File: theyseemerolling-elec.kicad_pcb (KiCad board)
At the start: 2 copper layers, 80 x 50 mm, 88 parts, among them IC2 L6205PD, J1 Conn_Encoder1, J2 Conn_Power_In, J3 Conn_SWD_UART, J4 Conn_Mot1, J5 Conn_Mot2, J6 Conn_Encoder2, J7 CAN_conn, J8 CAN_conn, Q1 BSS138, Q2 BSS138, Q3 BSS138, Q4 BSS138, Q5 BSS138, U1 STM32F303K8Tx, U2 LD1117S50TR_SOT223, U3 ACS711xLCTR-12AB, U4 ACS711xLCTR-12AB, U5 74HC00, U6 LD1117S33TR_SOT223, U7 TCAN332, U8 AT25SF041

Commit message: prettier
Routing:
- net +3V3: track 213.2 -> 210.8 mm
- net +5V: track 72.1 -> 70.4 mm
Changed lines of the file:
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@@
     (thickness 1.6)
     (drawings 13)
-    (tracks 573)
+    (tracks 575)
     (zones 0)
     (modules 88)
@@
   )
   (setup
-    (last_trace_width 0.25)
+    (last_trace_width 0.5)
     (user_trace_width 0.5)
     (user_trace_width 1)
@@
   (segment (start 165.8 72.4) (end 166.6 72.4) (width 1) (layer F.Cu) (net 15) (status 30))
   (segment (start 163.399989 69.999989) (end 165.8 72.4) (width 1) (layer F.Cu) (net 15) (status 20))
-  (via (at 132.19 78.3) (size 0.8) (drill 0.4) (layers F.Cu B.Cu) (net 16) (status 30))
-  (segment (start 127.975 68.8) (end 123.575 73.2) (width 0.5) (layer B.Cu) (net 16))
   (segment (start 143.8 63.8) (end 138.8 68.8) (width 0.5) (layer B.Cu) (net 16))
   (segment (start 143.8 63.8) (end 158.2 63.8) (width 0.5) (layer B.Cu) (net 16))
-  (segment (start 131.5375 78.3) (end 132.19 78.3) (width 0.25) (layer F.Cu) (net 16) (status 20))
-  (segment (start 130.1375 79.7) (end 131.5375 78.3) (width 0.25) (layer F.Cu) (net 16) (status 10))
-  (segment (start 130.1 79.7) (end 130.1375 79.7) (width 0.25) (layer F.Cu) (net 16) (status 30))
-  (segment (start 128.675 78.3) (end 132.19 78.3) (width 0.5) (layer B.Cu) (net 16))
-  (segment (start 123.575 73.2) (end 128.675 78.3) (width 0.5) (layer B.Cu) (net 16))
   (via (at 167.6 60.425) (size 0.8) (drill 0.4) (layers F.Cu B.Cu) (net 16) (status 30))
   (segment (start 166.1 60.905) (end 167.12 60.905) (width 0.5) (layer F.Cu) (net 16) (status 10))
@@
   (segment (start 127.975 64.425) (end 128.375 64.025) (width 0.5) (layer B.Cu) (net 16))
   (segment (start 128.375 64.025) (end 128.4 64.025) (width 0.5) (layer B.Cu) (net 16))
+  (segment (start 130.1 79.7) (end 130.1375 79.7) (width 0.25) (layer F.Cu) (net 16) (status 30))
+  (segment (start 130.1375 79.7) (end 131.5375 78.3) (width 0.25) (layer F.Cu) (net 16) (status 10))
+  (segment (start 131.5375 78.3) (end 132.19 78.3) (width 0.25) (layer F.Cu) (net 16) (status 20))
+  (via (at 130.1 79.7) (size 0.8) (drill 0.4) (layers F.Cu B.Cu) (net 16))
+  (segment (start 124.675216 73.975216) (end 130.1 79.4) (width 0.5) (layer B.Cu) (net 16))
+  (segment (start 130.1 79.4) (end 130.1 79.7) (width 0.5) (layer B.Cu) (net 16))
+  (segment (start 124.675216 72.099784) (end 127.975 68.8) (width 0.5) (layer B.Cu) (net 16))
+  (segment (start 124.675216 73.975216) (end 124.675216 72.099784) (width 0.5) (layer B.Cu) (net 16))
   (segment (start 107.725 62.2875) (end 107.2125 62.8) (width 1) (layer B.Cu) (net 17) (status 30))
   (segment (start 107.5 66.275) (end 107.425 66.2) (width 1) (layer B.Cu) (net 17) (status 30))
@@
   (segment (start 130.7 91.5375) (end 124.9625 91.5375) (width 1) (layer B.Cu) (net 19) (status 10))
   (segment (start 135.2625 91.5375) (end 135.2 91.6) (width 1) (layer B.Cu) (net 19) (status 30))
-  (segment (start 142 91.5375) (end 135.2625 91.5375) (width 1) (layer B.Cu) (net 19) (status 20))
   (segment (start 135.1375 91.5375) (end 135.2 91.6) (width 1) (layer B.Cu) (net 19) (status 30))
   (segment (start 130.7 91.5375) (end 135.1375 91.5375) (width 1) (layer B.Cu) (net 19) (status 30))
@@
   (segment (start 105.2 75.35) (end 105.2 73.2) (width 1) (layer B.Cu) (net 19) (status 10))
   (via (at 107 71.4) (size 0.8) (drill 0.4) (layers F.Cu B.Cu) (net 19) (status 30))
+  (segment (start 135.3625 91.4375) (end 135.2 91.6) (width 1) (layer B.Cu) (net 19))
+  (segment (start 140.2 91.4375) (end 135.3625 91.4375) (width 1) (layer B.Cu) (net 19))
   (segment (start 133.2 70.8) (end 125.6 78.4) (width 0.25) (layer F.Cu) (net 20))
   (segment (start 125.6 78.4) (end 124.75 78.4) (width 0.25) (layer F.Cu) (net 20) (status 20))

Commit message: Références
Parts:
- moved LOGO2 2.45 mm to (156.2, 59.8)

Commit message: Add text
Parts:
- moved C6 1.60 mm to (134.6, 64.6)
- moved D5 1.60 mm to (136.8, 64.6)
- moved Q1 1.60 mm to (131.4, 64.6)
- moved R16 1.60 mm to (128.4, 64.6)
- moved R2 1.60 mm to (135.8, 67.8)
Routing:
- net +3V3: track 210.8 -> 209.2 mm
- net /f3/ABOUT_DA_POWER: track 33.1 -> 32.4 mm
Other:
- board text added: "CAN"
- board text added: "Coder1"
- board text added: "Coder2"
- board text added: "Motor1"
- board text added: "Motor2"
- board text added: "Power In"
- board text added: "SWD+UART"

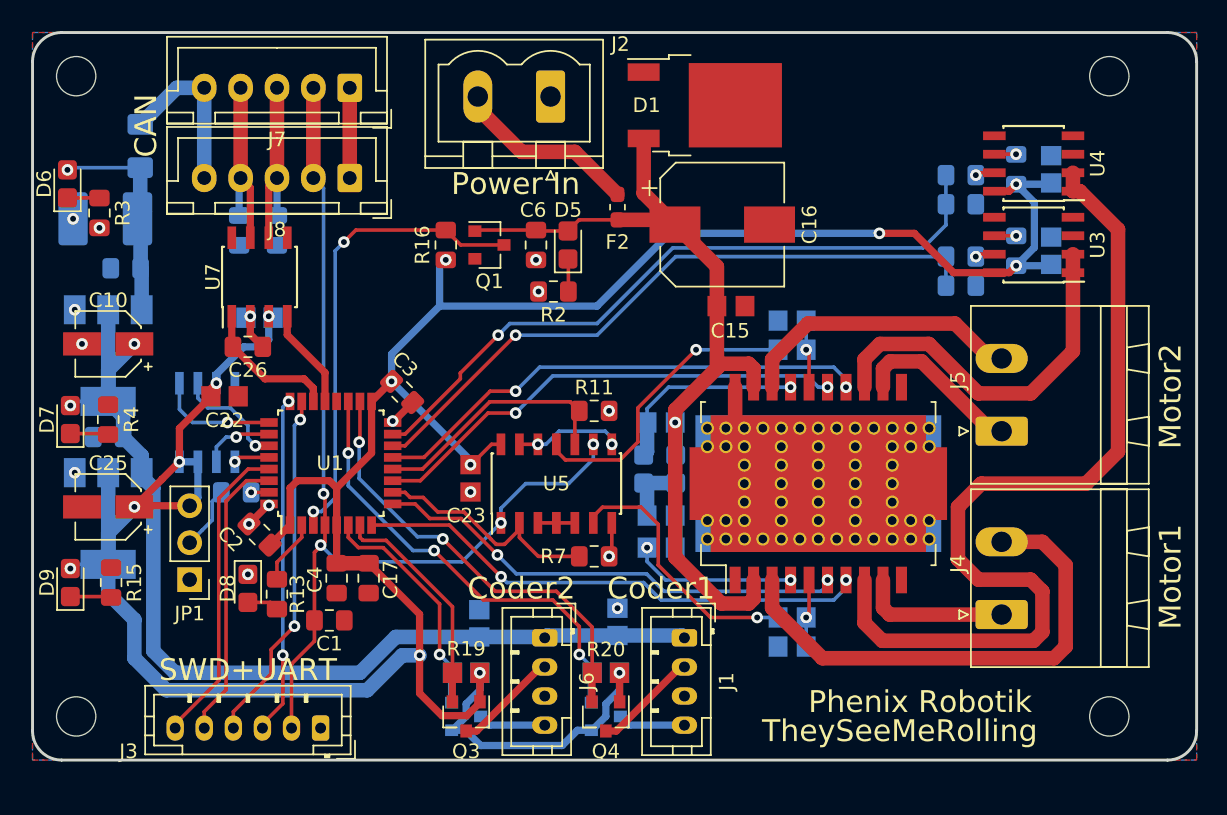
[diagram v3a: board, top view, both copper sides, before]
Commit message: Change connectors. reduce size.
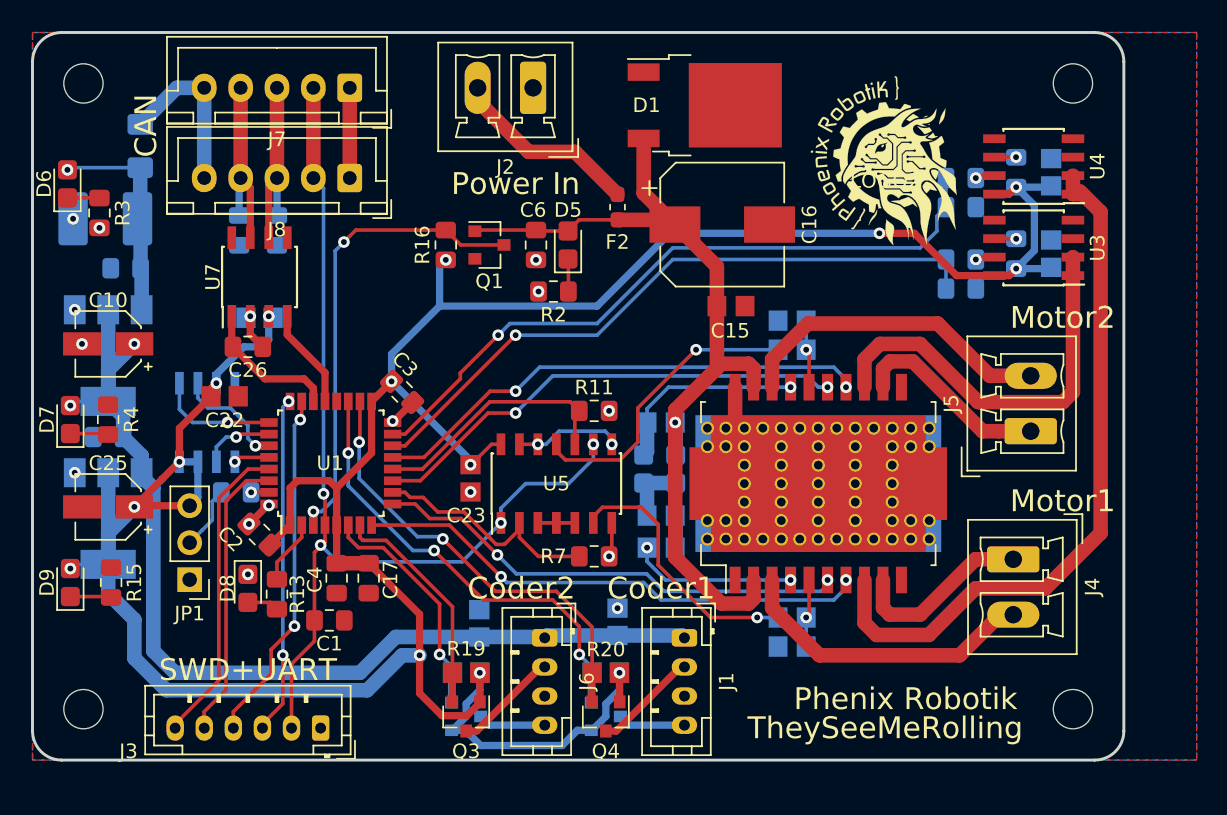
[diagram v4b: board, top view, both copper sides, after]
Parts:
- J2: footprint Connector_Phoenix_MSTB:PhoenixContact_MSTBVA_2,5_2-G_1x02_P5.00mm_Vertical -> Connector_Phoenix_MC:PhoenixContact_MCV_1,5_2-G-3.81_1x02_P3.81mm_Vertical
- J4, J5: footprint Connector_Phoenix_MSTB:PhoenixContact_MSTBA_2,5_2-G_1x02_P5.00mm_Horizontal -> Connector_Phoenix_MC:PhoenixContact_MCV_1,5_2-G-3.81_1x02_P3.81mm_Vertical
- LOGO2: moved to F.Cu
- moved J4 3.88 mm to (167.4, 86.2), turned to 270 degrees
- moved MK2 2.55 mm to (171.5, 53.5)
- moved MK3 2.55 mm to (171.5, 96.5)
- moved LOGO2 2.43 mm to (158.6, 60.2), turned to 0 degrees
- moved J5 2.00 mm to (168.6, 77.4)
- moved J2 1.34 mm to (134.4, 53.8)
- moved MK1 0.71 mm to (103.5, 53.5)
- moved MK4 0.71 mm to (103.5, 96.5)
- moved C20 0.20 mm to (170.0, 65.2)
- moved C21 0.20 mm to (170.0, 59.6)
- moved C9 0.20 mm to (163.8, 62.0)
- moved R14 0.20 mm to (163.8, 60.0)
- moved R5 0.20 mm to (167.6, 65.2)
- moved R6 0.20 mm to (167.6, 59.6)
- moved U3 0.20 mm to (168.8, 64.8)
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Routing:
- net Net-(IC2-Pad8): track 62.3 -> 48.2 mm
- net /DualDCDriver/M1-: track 34.5 -> 21.0 mm
- net /DualDCDriver/M2-: track 19.7 -> 22.2 mm
- net /DualDCDriver/M1+: track 10.3 -> 12.6 mm
- net Net-(IC2-Pad13): track 26.0 -> 28.1 mm
- net /DualDCDriver/M2+: track 11.6 -> 13.6 mm
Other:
- board size 80 x 50 mm -> 75 x 50 mm

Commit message: fix phoenix/phenix
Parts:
- LOGO2: footprint PhoenixRobotik:Logo_14,5mm -> PhenixRobotik:Logo_14,5mm
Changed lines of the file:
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@@
     )
   )
-  (module PhoenixRobotik:Logo_14,5mm (layer F.Cu)
+  (module PhenixRobotik:Logo_14,5mm (layer F.Cu)
     (at 158.6 60.2)
     (descr https://github.com/PhenixRobotik)

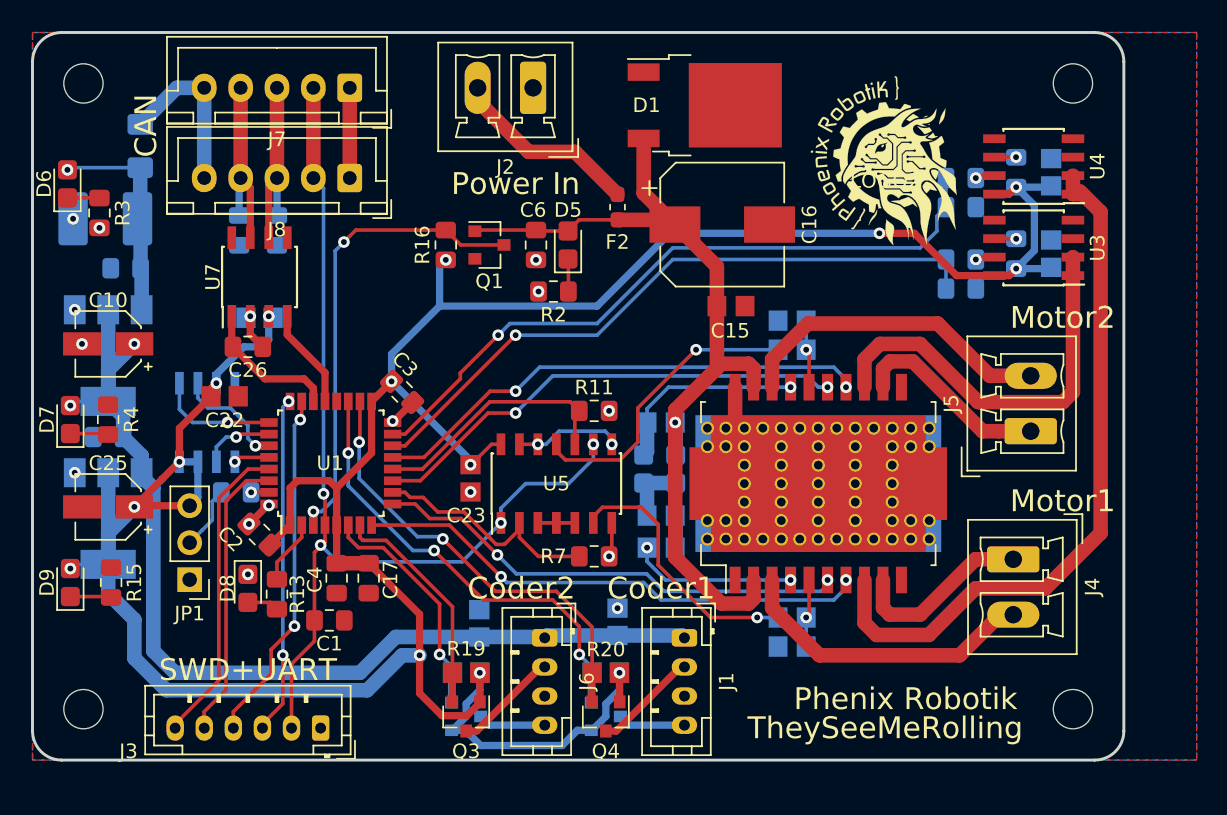
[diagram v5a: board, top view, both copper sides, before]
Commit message: Fix : use new footprints
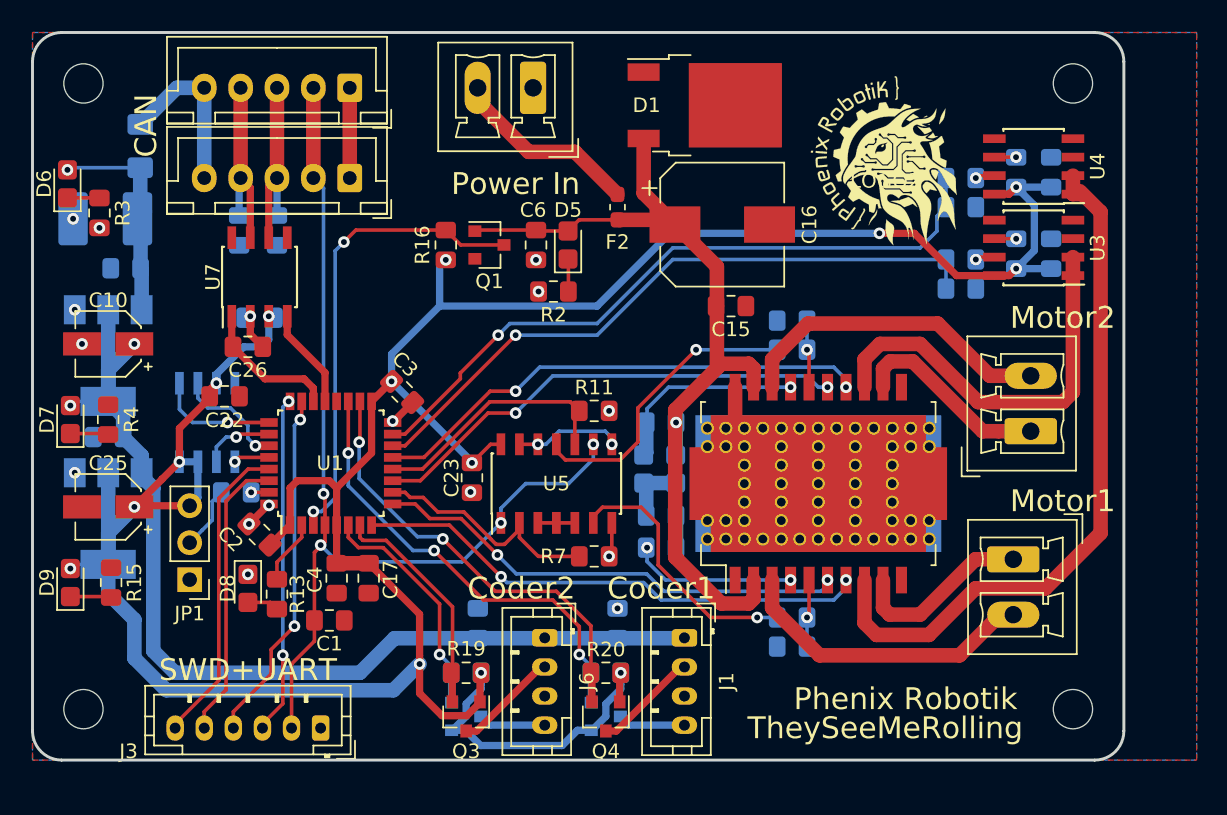
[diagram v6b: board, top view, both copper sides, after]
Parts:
- C11, C12, C13, C14, C15: footprint Capacitor_SMD:C_0805_2012Metric_Pad1.29x1.40mm_HandSolder -> Capacitor_SMD:C_0805_2012Metric_Pad1.15x1.40mm_HandSolder
- C18, C19, C20, C21, C22, C23, C24: footprint Capacitor_SMD:C_0805_2012Metric_Pad1.33x1.40mm_HandSolder -> Capacitor_SMD:C_0805_2012Metric_Pad1.15x1.40mm_HandSolder
- R10, R8, R9: footprint Resistor_SMD:R_0805_2012Metric_Pad1.29x1.40mm_HandSolder -> Resistor_SMD:R_0805_2012Metric_Pad1.15x1.40mm_HandSolder
- R18, R19, R20, R21: footprint Resistor_SMD:R_0805_2012Metric_Pad1.33x1.40mm_HandSolder -> Resistor_SMD:R_0805_2012Metric_Pad1.15x1.40mm_HandSolder
- moved C23 0.11 mm to (130.2, 80.6)
- moved C18 0.10 mm to (140.2, 90.6)
- moved C19 0.10 mm to (130.6, 90.6)

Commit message: Cleanup, check footprints, connect mounting holes to GND
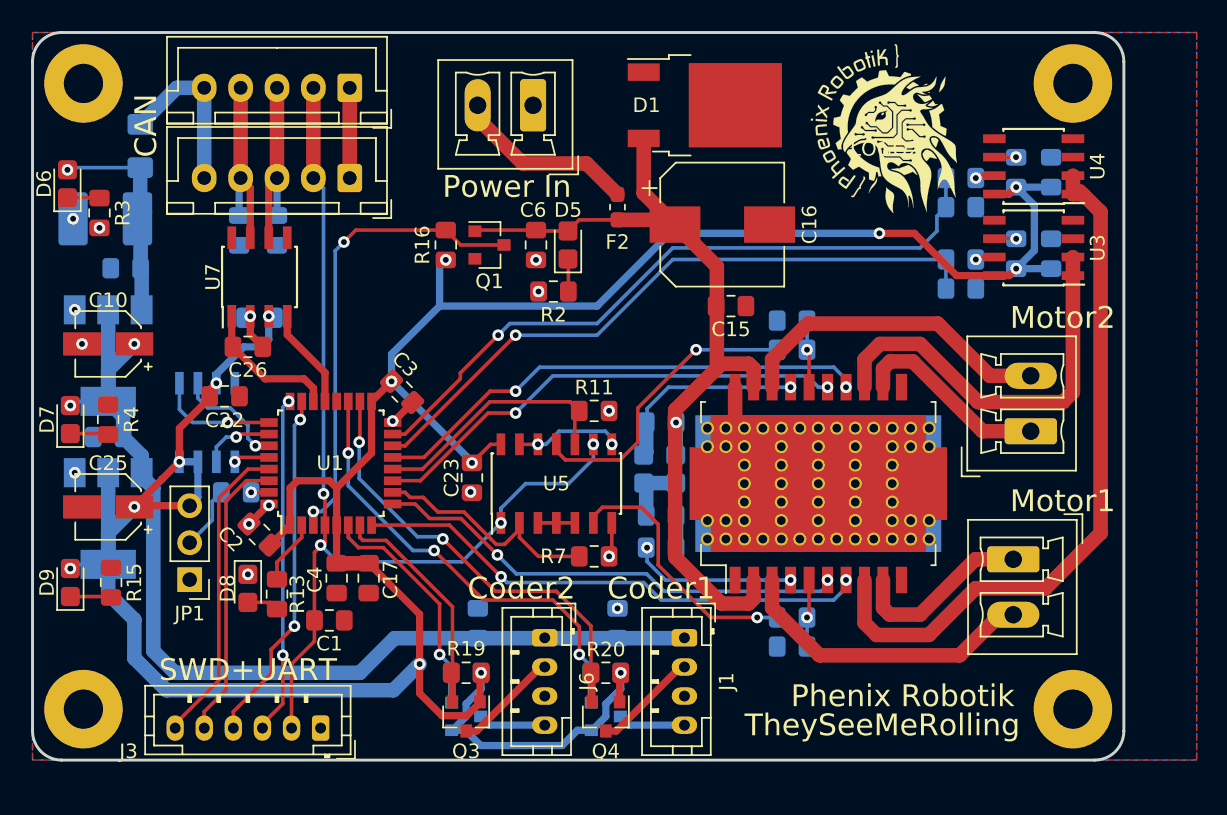
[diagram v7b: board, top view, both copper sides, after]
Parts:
- MK1, MK2, MK3, MK4: value Mounting_Hole -> MountingHole_Pad; footprint MountingHole:MountingHole_2.7mm_M2.5 -> MountingHole:MountingHole_2.7mm_M2.5_Pad
- moved LOGO2 2.20 mm to (158.6, 58.0)
- moved J2 1.20 mm to (134.4, 55.0)
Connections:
- MK1 pad 1: (no net) -> GND
- MK2 pad 1: (no net) -> GND
- MK3 pad 1: (no net) -> GND
- MK4 pad 1: (no net) -> GND

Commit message: Move silkscreen
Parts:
- moved LOGO1 10.9 mm to (157.4, 56.6)
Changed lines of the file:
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@@
   )
   (setup
-    (last_trace_width 1)
+    (last_trace_width 0.25)
     (user_trace_width 0.5)
     (user_trace_width 1)
@@
   )
   (module Symbol:OSHW-Logo_7.5x8mm_SilkScreen (layer B.Cu)
-    (at 146.6 58.4 180)
+    (at 157.4 56.6 180)
     (descr "Open Source Hardware Logo")
     (tags "Logo OSHW")
@@
     (fp_line (start -1 -0.6) (end 1 -0.6) (layer F.Fab) (width 0.1))
     (fp_line (start -1 0.6) (end -1 -0.6) (layer F.Fab) (width 0.1))
-    (pad 2 smd roundrect (at 1.025 0 135) (size 1.15 1.4) (layers F.Cu F.Paste F.Mask) (roundrect_rratio 0.217391)
+    (pad 2 smd roundrect (at 1.024999 0 135) (size 1.15 1.4) (layers F.Cu F.Paste F.Mask) (roundrect_rratio 0.217391)
       (net 7 GND))
-    (pad 1 smd roundrect (at -1.025 0 135) (size 1.15 1.4) (layers F.Cu F.Paste F.Mask) (roundrect_rratio 0.217391)
+    (pad 1 smd roundrect (at -1.024999 0 135) (size 1.15 1.4) (layers F.Cu F.Paste F.Mask) (roundrect_rratio 0.217391)
       (net 16 +3V3))
     (model ${KISYS3DMOD}/Capacitor_SMD.3dshapes/C_0805_2012Metric.wrl
@@
     (fp_line (start -1 -0.6) (end 1 -0.6) (layer F.Fab) (width 0.1))
     (fp_line (start -1 0.6) (end -1 -0.6) (layer F.Fab) (width 0.1))
-    (pad 2 smd roundrect (at 1.025 0 315) (size 1.15 1.4) (layers F.Cu F.Paste F.Mask) (roundrect_rratio 0.217391)
+    (pad 2 smd roundrect (at 1.024999 0 315) (size 1.15 1.4) (layers F.Cu F.Paste F.Mask) (roundrect_rratio 0.217391)
       (net 7 GND))
-    (pad 1 smd roundrect (at -1.025 0 315) (size 1.15 1.4) (layers F.Cu F.Paste F.Mask) (roundrect_rratio 0.217391)
+    (pad 1 smd roundrect (at -1.024999 0 315) (size 1.15 1.4) (layers F.Cu F.Paste F.Mask) (roundrect_rratio 0.217391)
       (net 16 +3V3))
     (model ${KISYS3DMOD}/Capacitor_SMD.3dshapes/C_0805_2012Metric.wrl
@@
   (gr_arc (start 173 98) (end 173 100) (angle -90) (layer Edge.Cuts) (width 0.2))
   (gr_arc (start 173 52) (end 175 52) (angle -90) (layer Edge.Cuts) (width 0.2))
-  (gr_text https://github.com/PhenixRobotik/theyseemerolling-elec (at 146.6 51.2) (layer B.SilkS)
+  (gr_text https://github.com/PhenixRobotik/theyseemerolling-elec (at 144.4 51.2) (layer B.SilkS)
     (effects (font (size 1.1 1.1) (thickness 0.25)) (justify mirror))
   )
